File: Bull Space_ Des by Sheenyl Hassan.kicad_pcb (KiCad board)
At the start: 2 copper layers, 45 x 77 mm, 36 parts, among them IC1 TEENSY_4.0, IC2 XB24CZ7PIT-004, J1 Screw_Terminal_01x06, Q1 AOI21357, Q2 2N7002, Q3 2N7002, Q4 2N7002, Q5 AOI21357, U1 VXO7803-1000, U2 Flight-Computer_Adafruit_GPS_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

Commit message: Digital wiring
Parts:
- moved U6 27.7 mm to (81.2, 73.2)
- moved U4 6.93 mm to (81.4, 79.8), turned to 90 degrees
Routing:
- net /ACT1: track 0.00 -> 50.1 mm, vias 0 -> 1
- net BUZZER: track 0.00 -> 46.7 mm, vias 0 -> 1
- net /ACT2: track 0.00 -> 46.0 mm, vias 0 -> 1
- net /SCK: track 38.6 -> 55.4 mm, vias 0 -> 2
- net +3V3: track 7.83 -> 16.7 mm, vias 1 -> 4
- net /MOSI: track 40.9 -> 46.9 mm, vias 2 -> 5
- net /MISO: track 43.1 -> 43.8 mm, vias 1 -> 0

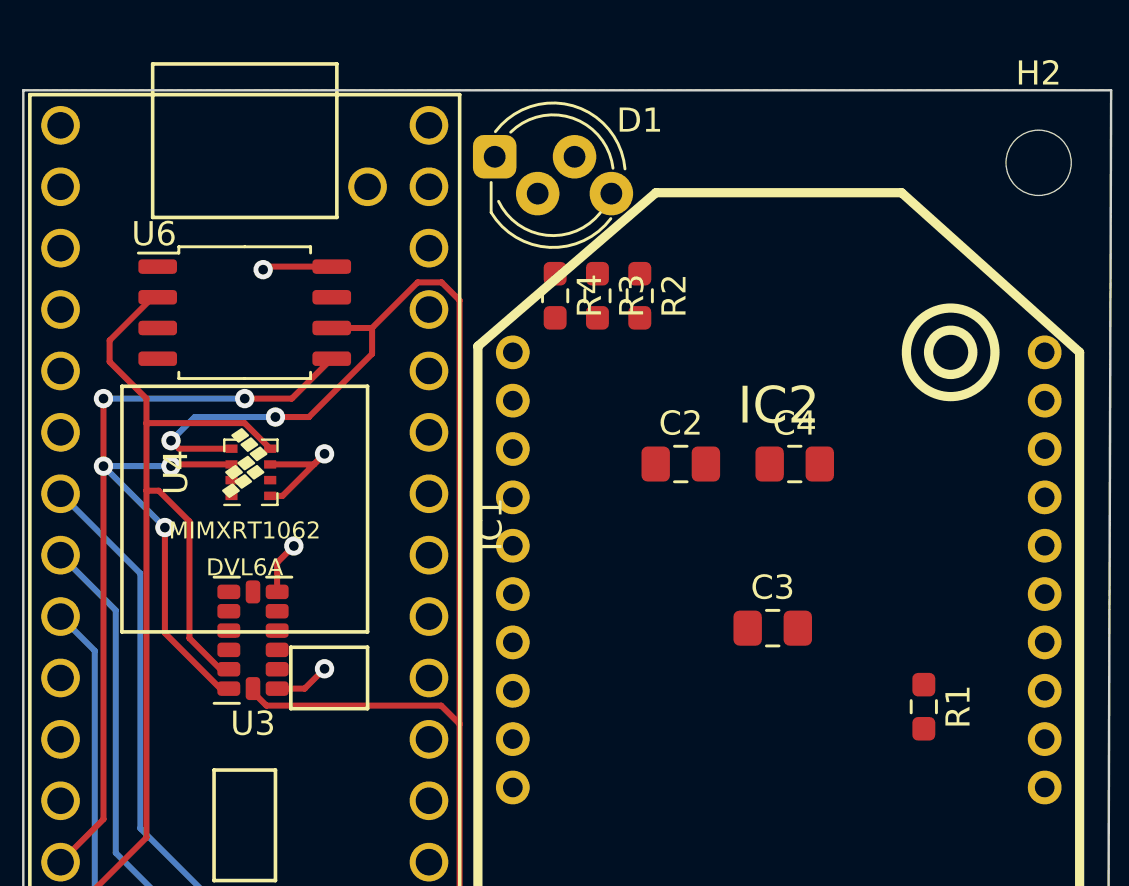
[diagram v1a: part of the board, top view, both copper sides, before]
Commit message: some capacitors and resistors traced
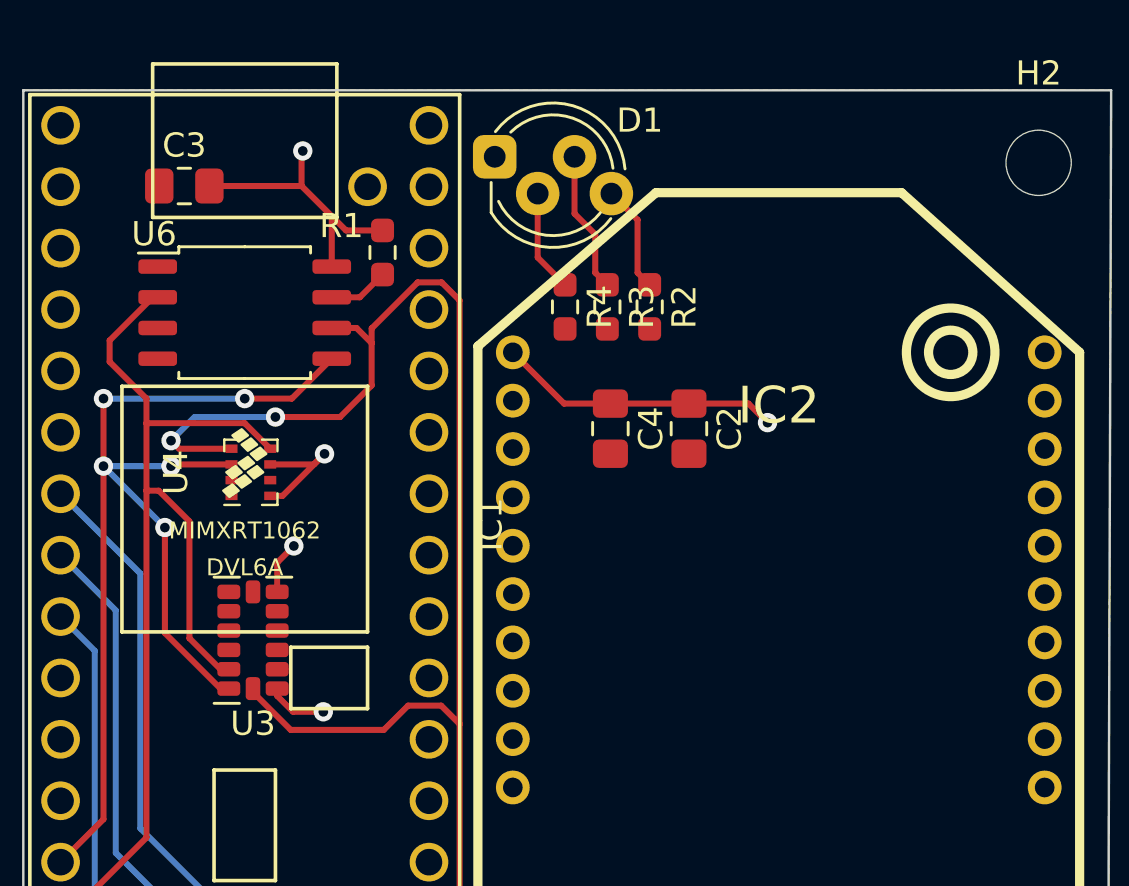
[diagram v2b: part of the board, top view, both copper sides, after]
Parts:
- moved C3 30.4 mm to (78.7, 68.0)
- moved R1 29.2 mm to (86.9, 70.7)
- moved C4 7.76 mm to (96.3, 78.0), turned to -90 degrees
- moved C2 1.50 mm to (99.5, 78.0), turned to -90 degrees
- moved R2 0.62 mm to (97.9, 73.0)
- moved R3 0.62 mm to (96.2, 73.0)
- moved R4 0.62 mm to (94.4, 73.0)
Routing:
- net +3V3: track 16.7 -> 37.2 mm, vias 4 -> 5
- net Net-(D1-Pad3): track 0.00 -> 5.86 mm
- net Net-(D1-Pad4): track 0.00 -> 4.43 mm
- net Net-(D1-Pad2): track 0.00 -> 4.24 mm
- net Net-(R1-Pad2): track 0.00 -> 2.49 mm
- net /SCK: track 55.4 -> 57.3 mm

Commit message: Minor optimizations
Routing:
- net /SCK: track 57.3 -> 45.6 mm, vias 2 -> 3
- net +3V3: track 37.2 -> 35.7 mm
- net /MISO: track 43.8 -> 45.2 mm
- net /MOSI: track 46.9 -> 48.0 mm

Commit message: Finished tracing (needs optimizing)
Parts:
- moved R2 11.7 mm to (109.2, 76.2)
- moved R3 11.5 mm to (107.2, 76.2)
- moved R4 11.3 mm to (105.3, 76.2)
- moved D1 3.66 mm to (95.2, 66.7)
- moved C2 1.52 mm to (98.8, 79.3)
- moved C4 1.31 mm to (96.3, 79.3)
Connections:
- IC1 pad 21: /XBEE-RX -> /GPS-RX
- IC1 pad 22: /XBEE-TX -> /GPS-TX
- IC1 pad 23: unconnected-(IC1-Pad23) -> LED-R
- IC1 pad 24: unconnected-(IC1-Pad24) -> LED-G
- IC1 pad 25: unconnected-(IC1-Pad25) -> LED-B
- IC1 pad 27: /GPS-RX -> /XBEE-RX
- IC1 pad 28: /GPS-TX -> /XBEE-TX
- IC1 pad 4: LED-R -> unconnected-(IC1-Pad4)
- IC1 pad 5: LED-G -> unconnected-(IC1-Pad5)
- IC1 pad 6: LED-B -> unconnected-(IC1-Pad6)
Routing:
- net LED-B: track 0.00 -> 32.2 mm
- net LED-G: track 0.00 -> 31.5 mm
- net LED-R: track 0.00 -> 30.9 mm
- net /GPS-TX: track 0.00 -> 29.0 mm
- net /GPS-RX: track 0.00 -> 27.9 mm
- net /FL-CS: track 0.00 -> 19.5 mm
- net /ADXL-CS: track 0.00 -> 18.2 mm, vias 0 -> 2
- net /BMP-CS: track 0.00 -> 15.6 mm, vias 0 -> 2
- net Net-(D1-Pad4): track 4.43 -> 13.5 mm
- net Net-(D1-Pad3): track 5.86 -> 14.7 mm
- net Net-(D1-Pad2): track 4.24 -> 12.7 mm
- net /XBEE-RX: track 0.00 -> 4.24 mm
- net /XBEE-TX: track 0.00 -> 4.01 mm
- net +3V3: track 35.7 -> 31.9 mm, vias 5 -> 4
- net /SCK: track 45.6 -> 46.6 mm

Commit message: Small optimizations
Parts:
- moved C2 3.55 mm to (98.0, 75.8)
- moved C4 3.55 mm to (95.5, 75.8)
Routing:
- net /MOSI: track 48.0 -> 22.4 mm, vias 5 -> 3
- net +3V3: track 31.9 -> 30.2 mm

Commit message: Connected some stuff to ground and 3V3
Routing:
- net GND: track 0.35 -> 11.6 mm, vias 0 -> 2
- net /MOSI: track 22.4 -> 33.2 mm, vias 3 -> 5
- net +3V3: track 30.2 -> 33.7 mm, vias 4 -> 5
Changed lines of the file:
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@@
   (segment (start 105.26 72.81) (end 103.36 70.91) (width 0.25) (layer "F.Cu") (net 3))
   (segment (start 105.26 75.2975) (end 105.26 72.81) (width 0.25) (layer "F.Cu") (net 3))
+  (segment (start 81.31 80.46) (end 81.66 80.11) (width 0.25) (layer "F.Cu") (net 6))
+  (segment (start 83.86 86.71) (end 83.86 86.936072) (width 0.25) (layer "F.Cu") (net 6))
+  (segment (start 83.86 86.936072) (end 82.846072 87.95) (width 0.25) (layer "F.Cu") (net 6))
+  (segment (start 83.86 85.81) (end 83.86 86.71) (width 0.25) (layer "F.Cu") (net 6))
+  (segment (start 83.6 85.55) (end 83.86 85.81) (width 0.25) (layer "F.Cu") (net 6))
+  (segment (start 81.31 80.949022) (end 82.170978 81.81) (width 0.25) (layer "F.Cu") (net 6))
+  (segment (start 81.31 80.46) (end 81.31 80.949022) (width 0.25) (layer "F.Cu") (net 6))
+  (segment (start 81.677 80.127) (end 82.212 80.127) (width 0.25) (layer "F.Cu") (net 6))
+  (segment (start 80.612 80.777) (end 80.993 80.777) (width 0.25) (layer "F.Cu") (net 6))
+  (segment (start 83.5 86.35) (end 83.86 86.71) (width 0.25) (layer "F.Cu") (net 6))
+  (segment (start 80.993 80.777) (end 81.31 80.46) (width 0.25) (layer "F.Cu") (net 6))
+  (segment (start 82.5 86.35) (end 83.5 86.35) (width 0.25) (layer "F.Cu") (net 6))
+  (segment (start 82.5 85.55) (end 83.6 85.55) (width 0.25) (layer "F.Cu") (net 6))
+  (segment (start 81.66 80.11) (end 81.677 80.127) (width 0.25) (layer "F.Cu") (net 6))
+  (segment (start 82.170978 81.81) (end 84.26 81.81) (width 0.25) (layer "F.Cu") (net 6))
   (segment (start 82.5 87.95) (end 82.846072 87.95) (width 0.25) (layer "F.Cu") (net 6))
+  (via (at 83.86 86.71) (size 0.8) (drill 0.4) (layers "F.Cu" "B.Cu") (net 6))
+  (via (at 84.26 81.81) (size 0.8) (drill 0.4) (layers "F.Cu" "B.Cu") (net 6))
   (segment (start 86.883 73.833) (end 87.26 74.21) (width 0.25) (layer "F.Cu") (net 7))
   (segment (start 85.46 93.21) (end 85.46 95.11) (width 0.25) (layer "F.Cu") (net 7))
@@
   (segment (start 84.758 69.208) (end 83.51 67.96) (width 0.25) (layer "F.Cu") (net 16))
   (segment (start 84.758 71.293) (end 84.758 69.208) (width 0.25) (layer "F.Cu") (net 16))
+  (segment (start 78.62 98.47) (end 78.62 97.15) (width 0.25) (layer "F.Cu") (net 16))
   (segment (start 83.66 80.11) (end 83.66 80.41) (width 0.25) (layer "F.Cu") (net 16))
   (segment (start 95.46 74.81) (end 97.96 74.81) (width 0.25) (layer "F.Cu") (net 16))
@@
   (segment (start 82.5 88.75) (end 82.5 89.05) (width 0.25) (layer "F.Cu") (net 16))
   (segment (start 79.6975 67.96) (end 83.51 67.96) (width 0.25) (layer "F.Cu") (net 16))
+  (segment (start 78.62 97.15) (end 80.16 95.61) (width 0.25) (layer "F.Cu") (net 16))
   (via (at 83.66 80.11) (size 0.8) (drill 0.4) (layers "F.Cu" "B.Cu") (net 16))
   (via (at 83.56 66.51) (size 0.8) (drill 0.4) (layers "F.Cu" "B.Cu") (net 16))
   (via (at 83.19 82.85) (size 0.8) (drill 0.4) (layers "F.Cu" "B.Cu") (net 16))
   (via (at 84.41 89.71) (size 0.8) (drill 0.4) (layers "F.Cu" "B.Cu") (net 16))
+  (via (at 80.16 95.61) (size 0.8) (drill 0.4) (layers "F.Cu" "B.Cu") (net 16))
   (segment (start 78.1425 134.62) (end 81.3 134.62) (width 0.5) (layer "F.Cu") (net 17))
   (segment (start 75.57 132.0475) (end 78.1425 134.62) (width 0.5) (layer "F.Cu") (net 17))
@@
   (segment (start 84.96 97.21) (end 88.78 93.39) (width 0.25) (layer "B.Cu") (net 20))
   (segment (start 84.96 106.476282) (end 84.96 97.21) (width 0.25) (layer "B.Cu") (net 20))
+  (segment (start 73.54 95.93) (end 74.74 95.93) (width 0.25) (layer "F.Cu") (net 24))
   (segment (start 77.856 82.310011) (end 77.856 86.452072) (width 0.25) (layer "F.Cu") (net 24))
   (segment (start 78.11 79.548) (end 78.181 79.477) (width 0.25) (layer "F.Cu") (net 24))
   (segment (start 84.758 75.103) (end 83.107 76.754) (width 0.25) (layer "F.Cu") (net 24))
+  (segment (start 79.56 90.91) (end 80.5 89.97) (width 0.25) (layer "F.Cu") (net 24))
   (segment (start 80.153928 88.75) (end 80.5 88.75) (width 0.25) (layer "F.Cu") (net 24))
+  (segment (start 80.5 89.97) (end 80.5 88.75) (width 0.25) (layer "F.Cu") (net 24))
+  (segment (start 74.74 95.93) (end 77.16 93.51) (width 0.25) (layer "F.Cu") (net 24))
   (segment (start 83.107 76.754) (end 81.158 76.754) (width 0.25) (layer "F.Cu") (net 24))
   (segment (start 77.856 86.452072) (end 80.153928 88.75) (width 0.25) (layer "F.Cu") (net 24))
@@
   (segment (start 78.181 79.477) (end 80.612 79.477) (width 0.25) (layer "F.Cu") (net 24))
   (via (at 81.158 76.754) (size 0.8) (drill 0.4) (layers "F.Cu" "B.Cu") (net 24))
+  (via (at 79.56 90.91) (size 0.8) (drill 0.4) (layers "F.Cu" "B.Cu") (net 24))
   (via (at 78.11 79.548) (size 0.8) (drill 0.4) (layers "F.Cu" "B.Cu") (net 24))
   (via (at 77.856011 82.31) (size 0.8) (drill 0.4) (layers "F.Cu" "B.Cu") (net 24))
+  (via (at 77.16 93.51) (size 0.8) (drill 0.4) (layers "F.Cu" "B.Cu") (net 24))
   (segment (start 77.96 79.698) (end 78.11 79.548) (width 0.25) (layer "B.Cu") (net 24))
   (segment (start 77.856011 82.31) (end 77.96 82.206011) (width 0.25) (layer "B.Cu") (net 24))
   (segment (start 81.158 76.754) (end 79.575886 76.754) (width 0.25) (layer "B.Cu") (net 24))
+  (segment (start 79.56 91.11) (end 79.56 90.91) (width 0.25) (layer "B.Cu") (net 24))
   (segment (start 78.11 78.219886) (end 78.11 79.548) (width 0.25) (layer "B.Cu") (net 24))
   (segment (start 79.575886 76.754) (end 78.11 78.219886) (width 0.25) (layer "B.Cu") (net 24))
+  (segment (start 77.16 93.51) (end 79.56 91.11) (width 0.25) (layer "B.Cu") (net 24))
   (segment (start 77.96 82.206011) (end 77.96 79.698) (width 0.25) (layer "B.Cu") (net 24))
   (segment (start 74.999029 93.39) (end 76.579029 91.81) (width 0.25) (layer "F.Cu") (net 25))
@@
   (segment (start 108.565 133.2925) (end 108.59 133.3175) (width 0.5) (layer "F.Cu") (net 69))
   (segment (start 106.05 136.19) (end 95.43 136.19) (width 0.5) (layer "F.Cu") (net 69))
-  (segment (start 95.43 136.19) (end 95.41 136.21) (width 0.5) (layer "F.Cu") (net 69))
   (segment (start 92.41 129.46) (end 90.81 127.86) (width 0.5) (layer "F.Cu") (net 69))
   (segment (start 106.05 133.2925) (end 108.565 133.2925) (width 0.5) (layer "F.Cu") (net 69))
+  (segment (start 95.43 136.19) (end 95.41 136.21) (width 0.5) (layer "F.Cu") (net 69))
   (segment (start 92.41 133.21) (end 92.41 129.46) (width 0.5) (layer "F.Cu") (net 69))
   (segment (start 90.81 127.86) (end 90.81 125.6725) (width 0.5) (layer "F.Cu") (net 69))

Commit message: Small changes
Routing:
- net GND: track 11.6 -> 44.0 mm, vias 2 -> 4
- net +3V3: track 33.7 -> 40.4 mm, vias 5 -> 6
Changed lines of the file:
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@@
   (segment (start 81.31 80.46) (end 81.66 80.11) (width 0.25) (layer "F.Cu") (net 6))
   (segment (start 83.86 86.71) (end 83.86 86.936072) (width 0.25) (layer "F.Cu") (net 6))
+  (segment (start 81.21 80.56) (end 81.21 80.849022) (width 0.25) (layer "F.Cu") (net 6))
   (segment (start 83.86 86.936072) (end 82.846072 87.95) (width 0.25) (layer "F.Cu") (net 6))
   (segment (start 83.86 85.81) (end 83.86 86.71) (width 0.25) (layer "F.Cu") (net 6))
+  (segment (start 93.815 116.265) (end 96.66 119.11) (width 0.25) (layer "F.Cu") (net 6))
   (segment (start 83.6 85.55) (end 83.86 85.81) (width 0.25) (layer "F.Cu") (net 6))
-  (segment (start 81.31 80.949022) (end 82.170978 81.81) (width 0.25) (layer "F.Cu") (net 6))
-  (segment (start 81.31 80.46) (end 81.31 80.949022) (width 0.25) (layer "F.Cu") (net 6))
+  (segment (start 81.21 80.56) (end 81.31 80.46) (width 0.25) (layer "F.Cu") (net 6))
   (segment (start 81.677 80.127) (end 82.212 80.127) (width 0.25) (layer "F.Cu") (net 6))
   (segment (start 80.612 80.777) (end 80.993 80.777) (width 0.25) (layer "F.Cu") (net 6))
   (segment (start 83.5 86.35) (end 83.86 86.71) (width 0.25) (layer "F.Cu") (net 6))
-  (segment (start 80.993 80.777) (end 81.31 80.46) (width 0.25) (layer "F.Cu") (net 6))
+  (segment (start 80.993 80.777) (end 81.21 80.56) (width 0.25) (layer "F.Cu") (net 6))
+  (segment (start 93.815 114.6) (end 93.815 116.265) (width 0.25) (layer "F.Cu") (net 6))
+  (segment (start 81.637489 81.276511) (end 83.518103 81.276511) (width 0.25) (layer "F.Cu") (net 6))
   (segment (start 82.5 86.35) (end 83.5 86.35) (width 0.25) (layer "F.Cu") (net 6))
+  (segment (start 84.46 80.334614) (end 84.46 77.01) (width 0.25) (layer "F.Cu") (net 6))
+  (segment (start 81.21 80.849022) (end 81.637489 81.276511) (width 0.25) (layer "F.Cu") (net 6))
   (segment (start 82.5 85.55) (end 83.6 85.55) (width 0.25) (layer "F.Cu") (net 6))
+  (segment (start 83.518103 81.276511) (end 84.46 80.334614) (width 0.25) (layer "F.Cu") (net 6))
   (segment (start 81.66 80.11) (end 81.677 80.127) (width 0.25) (layer "F.Cu") (net 6))
-  (segment (start 82.170978 81.81) (end 84.26 81.81) (width 0.25) (layer "F.Cu") (net 6))
   (segment (start 82.5 87.95) (end 82.846072 87.95) (width 0.25) (layer "F.Cu") (net 6))
+  (via (at 96.66 119.11) (size 0.8) (drill 0.4) (layers "F.Cu" "B.Cu") (net 6))
+  (via (at 84.46 77.01) (size 0.8) (drill 0.4) (layers "F.Cu" "B.Cu") (net 6))
   (via (at 83.86 86.71) (size 0.8) (drill 0.4) (layers "F.Cu" "B.Cu") (net 6))
-  (via (at 84.26 81.81) (size 0.8) (drill 0.4) (layers "F.Cu" "B.Cu") (net 6))
+  (via (at 102.86 128.71) (size 0.8) (drill 0.4) (layers "F.Cu" "B.Cu") (net 6))
+  (segment (start 96.66 119.11) (end 96.66 122.51) (width 0.25) (layer "B.Cu") (net 6))
+  (segment (start 96.66 122.51) (end 102.86 128.71) (width 0.25) (layer "B.Cu") (net 6))
+  (segment (start 88.58 67.99) (end 88.78 67.99) (width 0.25) (layer "B.Cu") (net 6))
+  (segment (start 84.46 77.01) (end 86.46 75.01) (width 0.25) (layer "B.Cu") (net 6))
+  (segment (start 86.46 70.11) (end 88.58 67.99) (width 0.25) (layer "B.Cu") (net 6))
+  (segment (start 86.46 75.01) (end 86.46 70.11) (width 0.25) (layer "B.Cu") (net 6))
   (segment (start 86.883 73.833) (end 87.26 74.21) (width 0.25) (layer "F.Cu") (net 7))
   (segment (start 85.46 93.21) (end 85.46 95.11) (width 0.25) (layer "F.Cu") (net 7))
@@
   (segment (start 83.427 79.477) (end 82.212 79.477) (width 0.25) (layer "F.Cu") (net 16))
   (segment (start 82.5 89.05) (end 83.16 89.71) (width 0.25) (layer "F.Cu") (net 16))
+  (segment (start 87.16 76.61) (end 87.16 75.6397) (width 0.25) (layer "F.Cu") (net 16))
   (segment (start 95.89 114.6) (end 95.89 111.13) (width 0.5) (layer "F.Cu") (net 16))
   (segment (start 83.51 66.56) (end 83.56 66.51) (width 0.25) (layer "F.Cu") (net 16))
   (segment (start 83.66 80.41) (end 83.293 80.777) (width 0.25) (layer "F.Cu") (net 16))
   (segment (start 83.51 67.96) (end 83.51 66.56) (width 0.25) (layer "F.Cu") (net 16))
+  (segment (start 88.314211 74.485489) (end 91.894749 74.485489) (width 0.25) (layer "F.Cu") (net 16))
   (segment (start 83.16 89.71) (end 84.41 89.71) (width 0.25) (layer "F.Cu") (net 16))
   (segment (start 95.89 111.13) (end 96.23 110.79) (width 0.5) (layer "F.Cu") (net 16))
+  (segment (start 87.16 75.6397) (end 88.314211 74.485489) (width 0.25) (layer "F.Cu") (net 16))
   (segment (start 95.46 74.81) (end 94.88176 74.81) (width 0.25) (layer "F.Cu") (net 16))
   (segment (start 84.758 69.208) (end 83.51 67.96) (width 0.25) (layer "F.Cu") (net 16))
   (segment (start 84.758 71.293) (end 84.758 69.208) (width 0.25) (layer "F.Cu") (net 16))
+  (segment (start 91.894749 74.485489) (end 92.24926 74.84) (width 0.25) (layer "F.Cu") (net 16))
   (segment (start 78.62 98.47) (end 78.62 97.15) (width 0.25) (layer "F.Cu") (net 16))
   (segment (start 83.66 80.11) (end 83.66 80.41) (width 0.25) (layer "F.Cu") (net 16))
@@
   (via (at 83.56 66.51) (size 0.8) (drill 0.4) (layers "F.Cu" "B.Cu") (net 16))
   (via (at 83.19 82.85) (size 0.8) (drill 0.4) (layers "F.Cu" "B.Cu") (net 16))
+  (via (at 87.16 76.61) (size 0.8) (drill 0.4) (layers "F.Cu" "B.Cu") (net 16))
   (via (at 84.41 89.71) (size 0.8) (drill 0.4) (layers "F.Cu" "B.Cu") (net 16))
   (via (at 80.16 95.61) (size 0.8) (drill 0.4) (layers "F.Cu" "B.Cu") (net 16))
